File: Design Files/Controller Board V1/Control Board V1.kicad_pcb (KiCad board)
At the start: 2 copper layers, 75 x 125 mm, 74 parts, among them J1 XT30PW-F, J2 XT30UPB-M, J3 XT30UPB-M, J4 XT30UPB-M, J5 XT30UPB-M, J6 XT30UPB-M, J7 XT30UPB-M, J8 SM04B-GHS-TB_LF__SN_-, Q1 LMG5200, U1 LMR51420XDDCR, U2 INA219BIDR, U3 INA219BIDR, U4 INA219BIDR, U5 SC0917

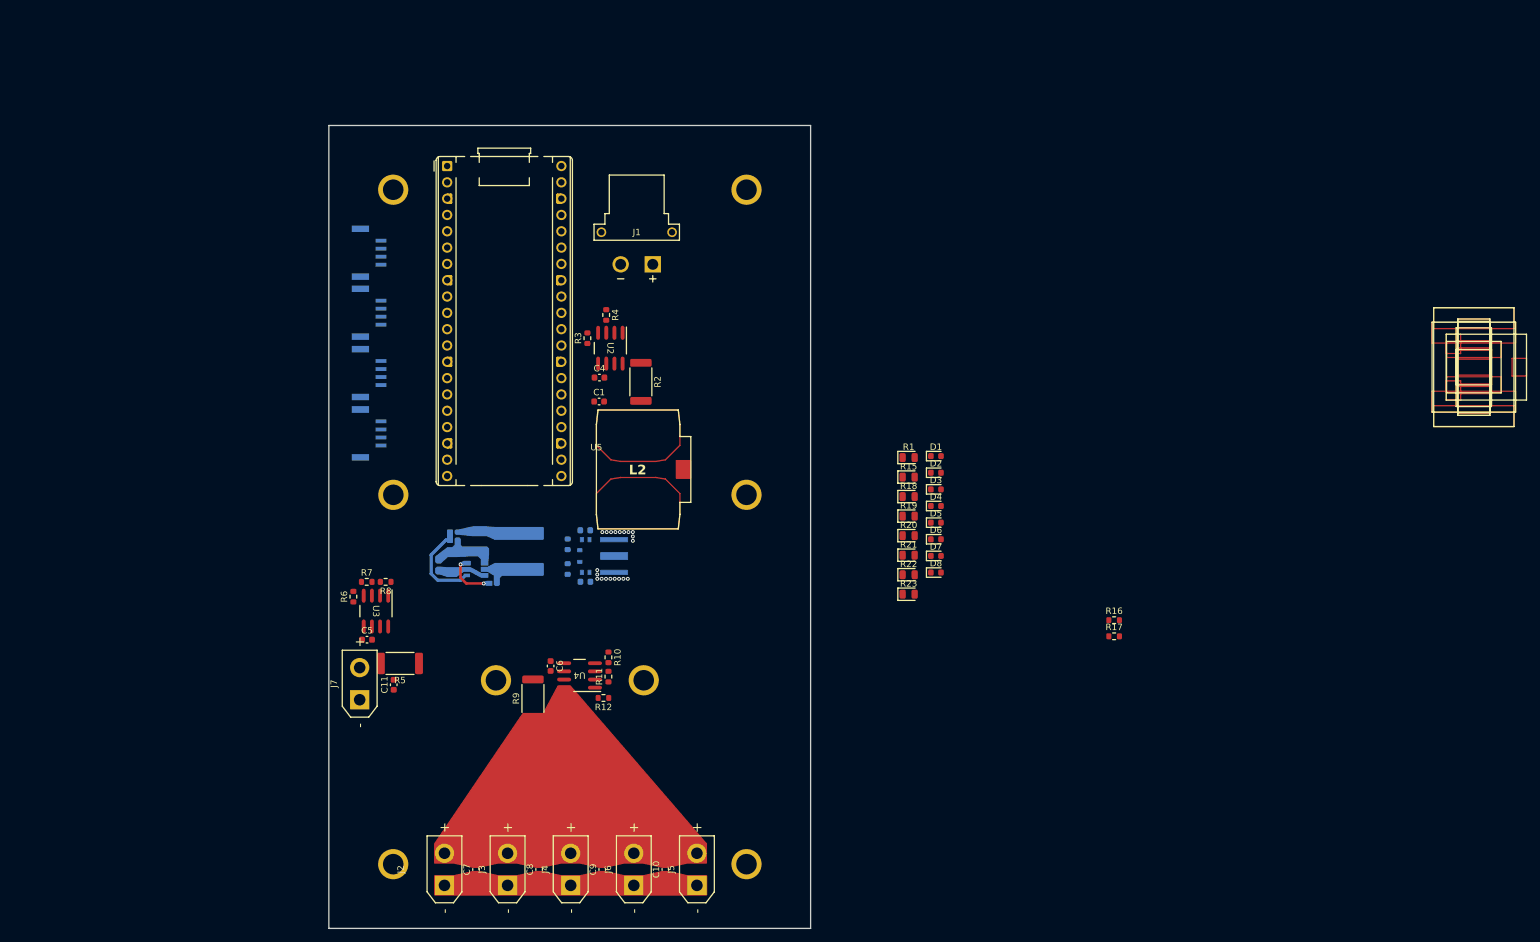
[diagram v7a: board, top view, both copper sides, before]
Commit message: Changed to four layer and added pours
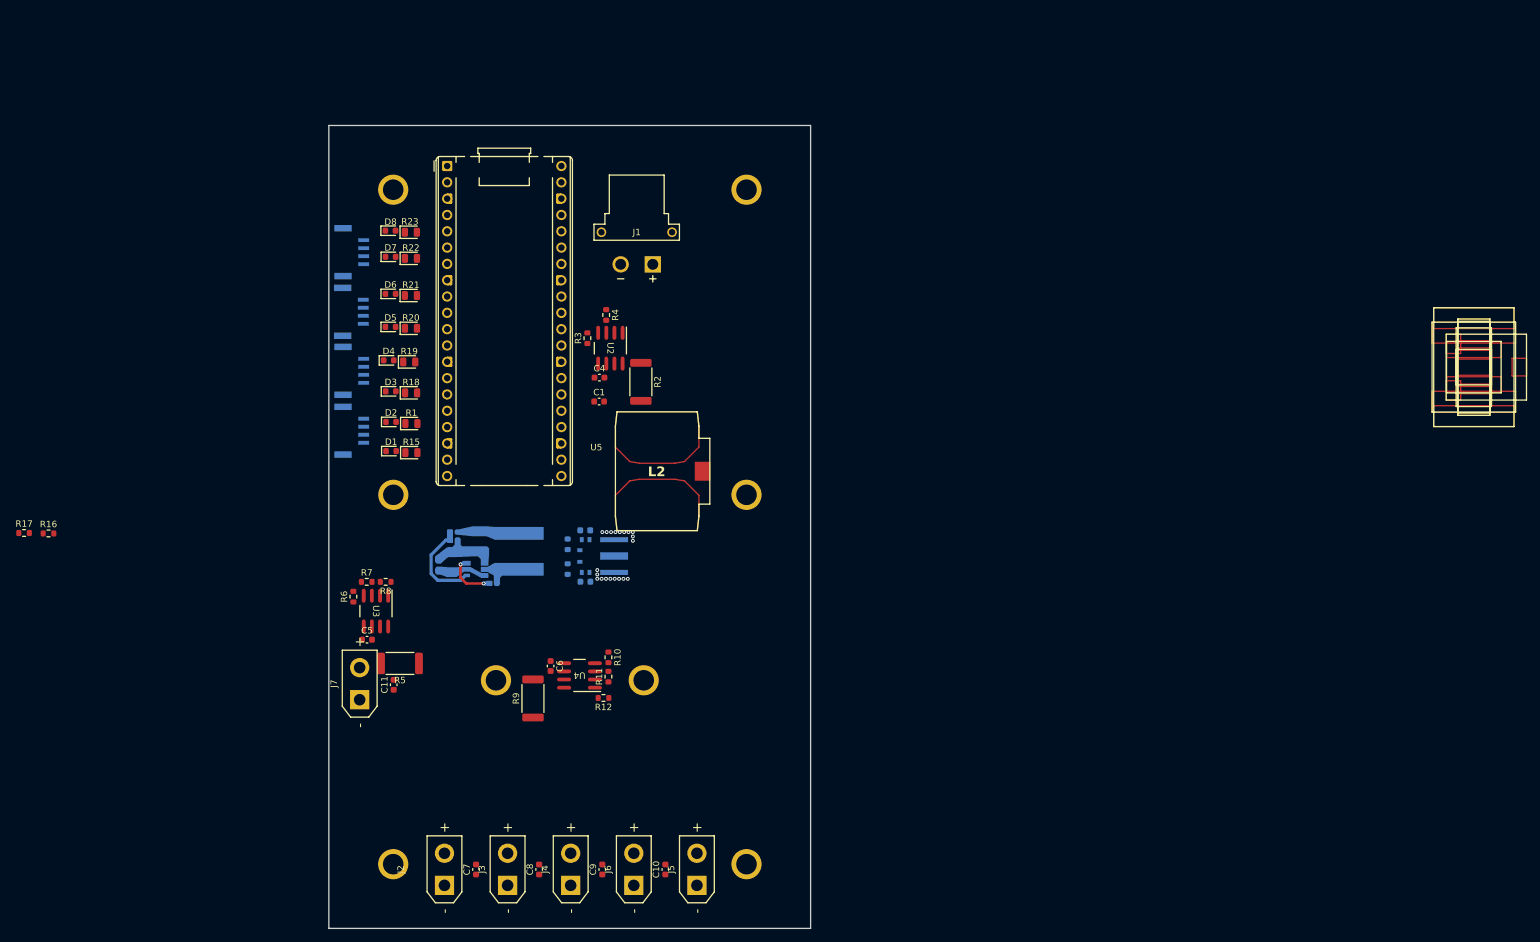
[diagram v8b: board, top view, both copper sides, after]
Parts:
- moved R17 170.5 mm to (15.1, 100.9)
- moved R16 166.4 mm to (18.9, 101.0)
- moved D8 100.2 mm to (72.1, 53.9)
- moved D7 96.8 mm to (72.1, 58.0)
- moved R23 95.8 mm to (75.3, 54.1)
- moved D6 93.1 mm to (72.1, 63.7)
- moved R22 91.8 mm to (75.3, 58.2)
- moved D5 90.2 mm to (72.1, 68.9)
- moved D4 88.2 mm to (71.8, 74.1)
- moved R21 87.4 mm to (75.3, 64.0)
- moved D3 86.2 mm to (72.1, 78.9)
- moved D2 85.2 mm to (72.2, 83.7)
- moved D1 84.8 mm to (72.2, 88.2)
- moved R20 83.9 mm to (75.3, 69.1)
- moved R19 81.4 mm to (75.0, 74.3)
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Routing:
- net Net-(L2-Pad1): vias 0 -> 5
- net (no net): vias 20 -> 15
- added copper zone on In2.Cu, net /24V_OUT
- added copper zone on In2.Cu, net 5V
- added copper zone on In1.Cu, net D_GND
- added copper zone on In1.Cu, net P_GND
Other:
- copper layers 2 -> 4
- board text added: "IGNORE THESE RESISTORS!!! YES, YOU! Don't touch them!"
- board text removed: "Put IO on this Side of Board!!!!!!!!!"
